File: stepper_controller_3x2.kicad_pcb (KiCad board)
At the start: 2 copper layers, 69.8 x 40.6 mm, 23 parts, among them P1 HEADER_02X05_SMD, P2 HEADER_02X05_SMD, P3 HEADER_02X05_SMD, T1 TERM_BLK_HDR_4POS_VERT_0.138IN, T2 TERM_BLK_HDR_4POS_VERT_0.138IN, T3 TERM_BLK_HDR_4POS_VERT_0.138IN, U1 TMC429, U2 26LS31, U3 MAX6817, U4 26LS31, U5 MAX6817, U6 26LS31, U7 MAX6817

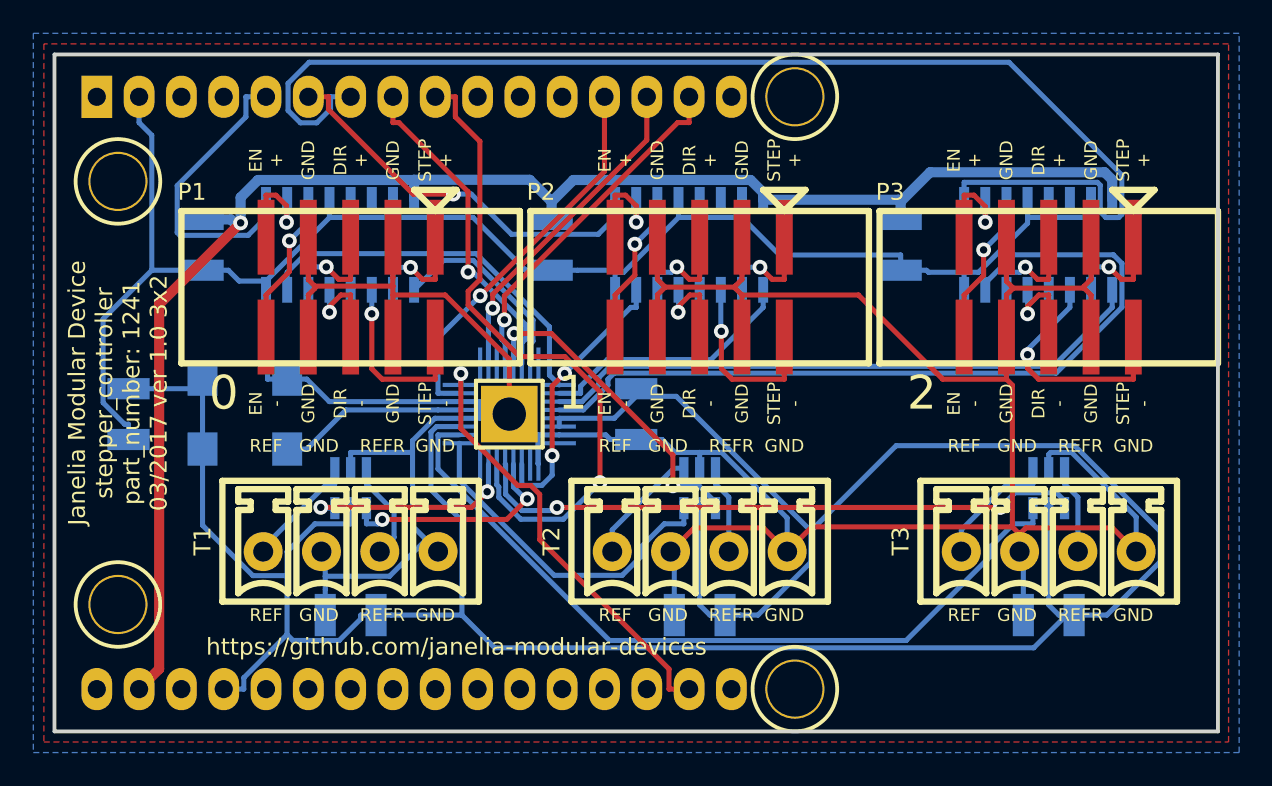
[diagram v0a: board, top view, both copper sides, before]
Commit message: Removed footprint.
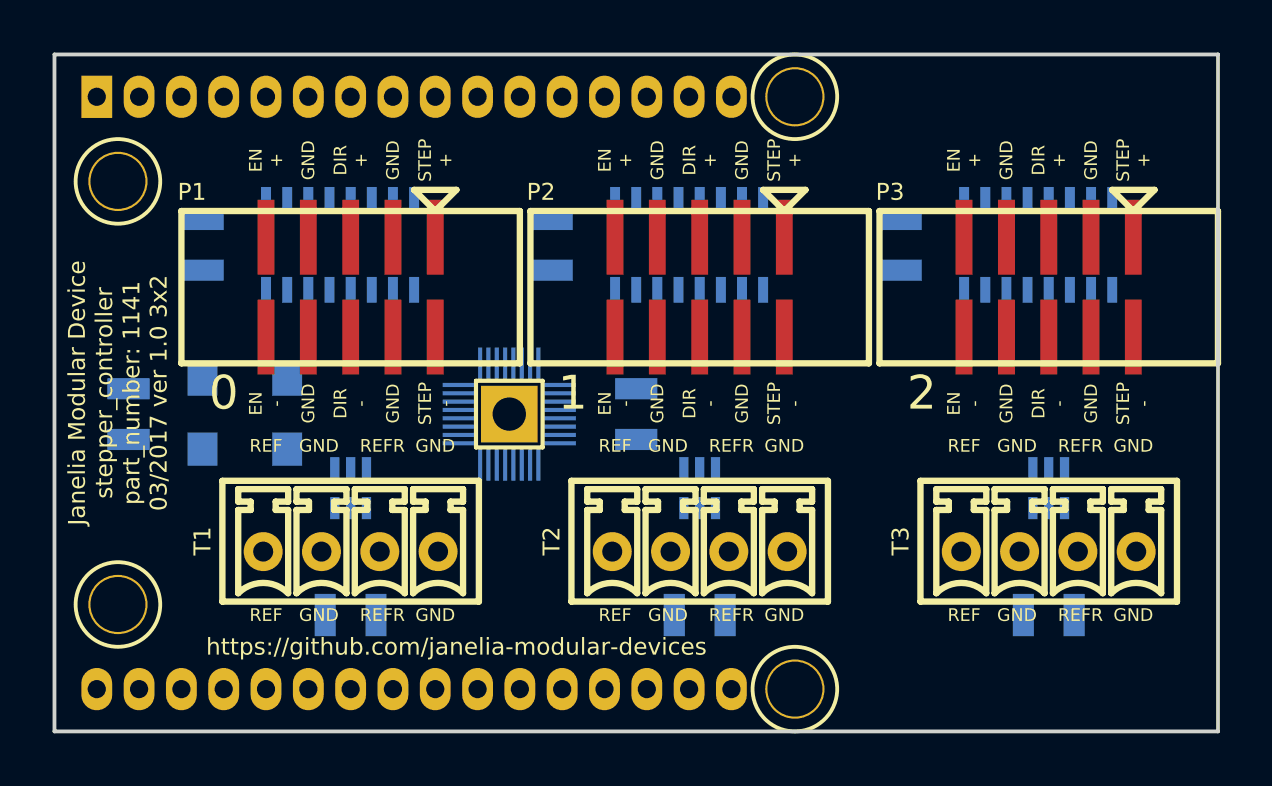
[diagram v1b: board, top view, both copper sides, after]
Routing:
- net GND: track 310.8 -> 0.00 mm
- net +3V3: track 175.5 -> 0.00 mm
- net VEE: track 94.5 -> 0.00 mm, vias 1 -> 0
- net /ENABLE_2: track 74.9 -> 0.00 mm
- net /tmc429_0/DIR_2: track 48.7 -> 0.00 mm
- net /tmc429_0/REF_2: track 47.5 -> 0.00 mm
- net /POSCOMP: track 39.7 -> 0.00 mm, vias 1 -> 0
- net /tmc429_0/REFR_2: track 36.9 -> 0.00 mm, vias 2 -> 0
- net /tmc429_0/STEP_2: track 36.8 -> 0.00 mm
- net /SCK: track 26.5 -> 0.00 mm, vias 1 -> 0
- net /ENABLE_1: track 23.7 -> 0.00 mm, vias 1 -> 0
- net /CS: track 23.2 -> 0.00 mm, vias 1 -> 0
- net /tmc429_0/DIR_0: track 22.8 -> 0.00 mm
- net /MISO: track 21.2 -> 0.00 mm, vias 1 -> 0
- net /tmc429_0/REF_1: track 20.6 -> 0.00 mm
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- removed copper zone on B.Cu, net GND
- removed copper zone on F.Cu, net GND
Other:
- board text added: "Janelia Modular Device stepper_controller part_number: 1141 03/2017 ver 1.0 3x2"
- board text removed: "Janelia Modular Device stepper_controller part_number: 1241 03/2017 ver 1.0 3x2"

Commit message: First attempt at layout.
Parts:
- removed P1, P2, P3: HEADER_02X05_SMD, stepper_controller_3x2:HEADER_02x05_SMD
- added C10: 0.1uF_0805, stepper_controller_3x2:SM0805, F.Cu at (189.3, 126.9)
- added C11: 0.47uF_0805, stepper_controller_3x2:SM0805, F.Cu at (189.6, 123.1)
- added C12: 0.1uF, stepper_controller_3x2:SM1210, F.Cu at (202.4, 111.5)
- added C13: 0.1uF_0805, stepper_controller_3x2:SM0805, F.Cu at (184.9, 98.5)
- added C14: 0.1uF_0805, stepper_controller_3x2:SM0805, F.Cu at (210.0, 86.7)
- added C15: 0.1uF_0805, stepper_controller_3x2:SM0805, F.Cu at (177.5, 98.5)
- added C16: 0.47uF_0805, stepper_controller_3x2:SM0805, F.Cu at (169.8, 98.5)
- added C17: 0.1uF, stepper_controller_3x2:SM1210, F.Cu at (209.0, 91.5)
- added C9: 0.1uF_0805, stepper_controller_3x2:SM0805, F.Cu at (203.4, 107.0)
- added T4: TERM_BLK_HDR_4POS_VERT_0.138IN, stepper_controller_3x2:TERM_BLK_HDR_4POS_VERT_0.138IN, F.Cu at (124.5, 98.4)
- added T5: TERM_BLK_HDR_4POS_VERT_0.150IN, stepper_controller_3x2:TERM_BLK_HDR_4POS_VERT_0.150IN, F.Cu at (145.4, 80.0)
- added T6: TERM_BLK_HDR_4POS_VERT_0.138IN, stepper_controller_3x2:TERM_BLK_HDR_4POS_VERT_0.138IN, F.Cu at (145.4, 98.4)
- C3, C5: value 0.1uF -> 0.1uF_0805; footprint stepper_controller_3x2:SM1210 -> stepper_controller_3x2:SM0805; moved to F.Cu
- C4, C8: value 0.1uF -> 0.1uF_0805; footprint stepper_controller_3x2:SM1210 -> stepper_controller_3x2:SM0805
- C6: value 0.1uF -> 0.47uF_0805; footprint stepper_controller_3x2:SM1210 -> stepper_controller_3x2:SM0805
- C7: moved to F.Cu
- T1, T3: value TERM_BLK_HDR_4POS_VERT_0.138IN -> TERM_BLK_HDR_4POS_VERT_0.150IN; footprint stepper_controller_3x2:TERM_BLK_HDR_4POS_VERT_0.138IN -> stepper_controller_3x2:TERM_BLK_HDR_4POS_VERT_0.150IN
- U2, U4: value 26LS31 -> TMC260; footprint stepper_controller_3x2:SOIC_16_0.154IN -> stepper_controller_3x2:TMC260+261; moved to F.Cu
- U6: value 26LS31 -> TMC260; footprint stepper_controller_3x2:SOIC_16_0.154IN -> stepper_controller_3x2:TMC260+261
- moved C3 151.4 mm to (245.9, 74.2), turned to 0 degrees
- moved U2 131.9 mm to (235.3, 77.3), turned to 0 degrees
- moved C5 130.7 mm to (245.9, 70.6), turned to 0 degrees
- moved C7 116.1 mm to (252.3, 71.5), turned to 0 degrees
- moved U4 76.2 mm to (192.8, 113.7), turned to 0 degrees
- moved T3 27.9 mm to (124.5, 80.0)
- moved U6 27.8 mm to (129.5, 57.1), turned to 0 degrees
- moved T1 21.0 mm to (103.5, 77.5)
- moved T2 21.0 mm to (103.5, 98.4)
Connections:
- net /CS renamed /CS_429
- net /tmc429_0/REFR_0 renamed /tmc429_tmc26x_0/REFR_0
- net /tmc429_0/REFR_1 renamed /tmc429_tmc26x_0/REFR_1
- net /tmc429_0/REFR_2 renamed /tmc429_tmc26x_0/REFR_2
- net /tmc429_0/REF_0 renamed /tmc429_tmc26x_0/REF_0
- net /tmc429_0/REF_1 renamed /tmc429_tmc26x_0/REF_1
- net /tmc429_0/REF_2 renamed /tmc429_tmc26x_0/REF_2
- C3 pad 1: VEE -> +3V3
- C4 pad 1: +3V3 -> VDD
- C5 pad 1: VEE -> VDD
- C5 pad 2: GND -> Net-(C5-Pad2)
- C6 pad 1: +3V3 -> Net-(C6-Pad1)
- C7 pad 1: VEE -> +3V3
- MDB1 pad 14: (no net) -> /CS_26X_0
- MDB1 pad 15: (no net) -> /CS_26X_1
- MDB1 pad 16: (no net) -> /CS_26X_2
- MDB1 pad 17: (no net) -> /SG_0
- MDB1 pad 18: (no net) -> /SG_1
- MDB1 pad 19: (no net) -> /SG_2
- MDB1 pad VDD: (no net) -> VDD
- MDB1 pad VEE: VEE -> (no net)
- T1 pad 1: /tmc429_0/stepper_0/REF_B -> /tmc429_tmc26x_0/stepper_0/A_+
- T1 pad 2: GND -> /tmc429_tmc26x_0/stepper_0/A_-
- T1 pad 3: /tmc429_0/stepper_0/REFR_B -> /tmc429_tmc26x_0/stepper_0/B_+
- T1 pad 4: GND -> /tmc429_tmc26x_0/stepper_0/B_-
- T2 pad 1: /tmc429_0/stepper_1/REF_B -> /tmc429_tmc26x_0/stepper_0/REF_B
- T2 pad 3: /tmc429_0/stepper_1/REFR_B -> /tmc429_tmc26x_0/stepper_0/REFR_B
- T3 pad 1: /tmc429_0/stepper_2/REF_B -> /tmc429_tmc26x_0/stepper_1/A_+
- T3 pad 2: GND -> /tmc429_tmc26x_0/stepper_1/A_-
- T3 pad 3: /tmc429_0/stepper_2/REFR_B -> /tmc429_tmc26x_0/stepper_1/B_+
- T3 pad 4: GND -> /tmc429_tmc26x_0/stepper_1/B_-
- U1 pad 15: /tmc429_0/STEP_0 -> /tmc429_tmc26x_0/STEP_0
- U1 pad 17: /tmc429_0/DIR_0 -> /tmc429_tmc26x_0/DIR_0
- U1 pad 18: /tmc429_0/STEP_1 -> /tmc429_tmc26x_0/STEP_1
- U1 pad 19: /tmc429_0/STEP_2 -> /tmc429_tmc26x_0/STEP_2
- U1 pad 20: /tmc429_0/DIR_2 -> /tmc429_tmc26x_0/DIR_2
- U1 pad 27: /tmc429_0/DIR_1 -> /tmc429_tmc26x_0/DIR_1
- U2 pad 1: /tmc429_0/STEP_0 -> (no net)
- U2 pad 10: /tmc429_0/stepper_0/ENABLE_+ -> /tmc429_tmc26x_0/stepper_0/A_-
- U2 pad 12: GND -> (no net)
- U2 pad 13: (no net) -> Net-(C6-Pad1)
- U2 pad 14: (no net) -> /MISO
- U2 pad 15: GND -> /MOSI
- U2 pad 16: VEE -> /SCK
- U2 pad 2: /tmc429_0/stepper_0/STEP_+ -> /tmc429_tmc26x_0/stepper_0/A_+
- U2 pad 4: (no net) -> VDD
- U2 pad 5: /tmc429_0/stepper_0/DIR_- -> /tmc429_tmc26x_0/stepper_0/A_-
- U2 pad 7: /tmc429_0/DIR_0 -> /tmc429_tmc26x_0/stepper_0/A_+
- U2 pad 9: /ENABLE_0 -> (no net)
- U3 pad 1: /tmc429_0/stepper_0/REF_B -> /tmc429_tmc26x_0/stepper_0/REF_B
- U3 pad 3: /tmc429_0/stepper_0/REFR_B -> /tmc429_tmc26x_0/stepper_0/REFR_B
- U4 pad 1: /tmc429_0/STEP_1 -> (no net)
- U4 pad 10: /tmc429_0/stepper_1/ENABLE_+ -> /tmc429_tmc26x_0/stepper_1/A_-
- U4 pad 12: GND -> (no net)
- U4 pad 13: (no net) -> Net-(C11-Pad1)
- U4 pad 14: (no net) -> /MISO
- U4 pad 15: GND -> /MOSI
- U4 pad 16: VEE -> /SCK
- U4 pad 2: /tmc429_0/stepper_1/STEP_+ -> /tmc429_tmc26x_0/stepper_1/A_+
- U4 pad 4: (no net) -> VDD
- U4 pad 5: /tmc429_0/stepper_1/DIR_- -> /tmc429_tmc26x_0/stepper_1/A_-
- U4 pad 7: /tmc429_0/DIR_1 -> /tmc429_tmc26x_0/stepper_1/A_+
- U4 pad 9: /ENABLE_1 -> (no net)
- U5 pad 1: /tmc429_0/stepper_1/REF_B -> /tmc429_tmc26x_0/stepper_1/REF_B
- U5 pad 3: /tmc429_0/stepper_1/REFR_B -> /tmc429_tmc26x_0/stepper_1/REFR_B
- U6 pad 1: /tmc429_0/STEP_2 -> (no net)
- U6 pad 10: /tmc429_0/stepper_2/ENABLE_+ -> /tmc429_tmc26x_0/stepper_2/A_-
- U6 pad 12: GND -> (no net)
- U6 pad 13: (no net) -> Net-(C16-Pad1)
- U6 pad 14: (no net) -> /MISO
- U6 pad 15: GND -> /MOSI
- U6 pad 16: VEE -> /SCK
- U6 pad 2: /tmc429_0/stepper_2/STEP_+ -> /tmc429_tmc26x_0/stepper_2/A_+
- U6 pad 4: (no net) -> VDD
- U6 pad 5: /tmc429_0/stepper_2/DIR_- -> /tmc429_tmc26x_0/stepper_2/A_-
- U6 pad 7: /tmc429_0/DIR_2 -> /tmc429_tmc26x_0/stepper_2/A_+
- U6 pad 9: /ENABLE_2 -> (no net)
- U7 pad 1: /tmc429_0/stepper_2/REF_B -> /tmc429_tmc26x_0/stepper_2/REF_B
- U7 pad 3: /tmc429_0/stepper_2/REFR_B -> /tmc429_tmc26x_0/stepper_2/REFR_B
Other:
- board text removed: "DIR +"
- board text removed: "DIR -"
- board text removed: "EN +"
- board text removed: "EN -"
- board text removed: "STEP +"
- board text removed: "STEP -"

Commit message: tmc26x -> driver.
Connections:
- net /tmc429_tmc26x_0/DIR_0 renamed /tmc429_driver_0/DIR_0
- net /tmc429_tmc26x_0/DIR_1 renamed /tmc429_driver_0/DIR_1
- net /tmc429_tmc26x_0/DIR_2 renamed /tmc429_driver_0/DIR_2
- net /tmc429_tmc26x_0/REFR_0 renamed /tmc429_driver_0/REFR_0
- net /tmc429_tmc26x_0/REFR_1 renamed /tmc429_driver_0/REFR_1
- net /tmc429_tmc26x_0/REFR_2 renamed /tmc429_driver_0/REFR_2
- net /tmc429_tmc26x_0/REF_0 renamed /tmc429_driver_0/REF_0
- net /tmc429_tmc26x_0/REF_1 renamed /tmc429_driver_0/REF_1
- net /tmc429_tmc26x_0/REF_2 renamed /tmc429_driver_0/REF_2
- net /tmc429_tmc26x_0/STEP_0 renamed /tmc429_driver_0/STEP_0
- net /tmc429_tmc26x_0/STEP_1 renamed /tmc429_driver_0/STEP_1
- net /tmc429_tmc26x_0/STEP_2 renamed /tmc429_driver_0/STEP_2
- net /tmc429_tmc26x_0/stepper_0/A_+ renamed /tmc429_driver_0/stepper_0/A_+
- net /tmc429_tmc26x_0/stepper_0/A_- renamed /tmc429_driver_0/stepper_0/A_-
- net /tmc429_tmc26x_0/stepper_0/B_+ renamed /tmc429_driver_0/stepper_0/B_+
- net /tmc429_tmc26x_0/stepper_0/B_- renamed /tmc429_driver_0/stepper_0/B_-
- net /tmc429_tmc26x_0/stepper_0/REFR_B renamed /tmc429_driver_0/stepper_0/REFR_B
- net /tmc429_tmc26x_0/stepper_0/REF_B renamed /tmc429_driver_0/stepper_0/REF_B
- net /tmc429_tmc26x_0/stepper_1/A_+ renamed /tmc429_driver_0/stepper_1/A_+
- net /tmc429_tmc26x_0/stepper_1/A_- renamed /tmc429_driver_0/stepper_1/A_-
- net /tmc429_tmc26x_0/stepper_1/B_+ renamed /tmc429_driver_0/stepper_1/B_+
- net /tmc429_tmc26x_0/stepper_1/B_- renamed /tmc429_driver_0/stepper_1/B_-
- net /tmc429_tmc26x_0/stepper_1/REFR_B renamed /tmc429_driver_0/stepper_1/REFR_B
- net /tmc429_tmc26x_0/stepper_1/REF_B renamed /tmc429_driver_0/stepper_1/REF_B
- net /tmc429_tmc26x_0/stepper_2/A_+ renamed /tmc429_driver_0/stepper_2/A_+
- net /tmc429_tmc26x_0/stepper_2/A_- renamed /tmc429_driver_0/stepper_2/A_-
- net /tmc429_tmc26x_0/stepper_2/B_+ renamed /tmc429_driver_0/stepper_2/B_+
- net /tmc429_tmc26x_0/stepper_2/B_- renamed /tmc429_driver_0/stepper_2/B_-
- net /tmc429_tmc26x_0/stepper_2/REFR_B renamed /tmc429_driver_0/stepper_2/REFR_B
- net /tmc429_tmc26x_0/stepper_2/REF_B renamed /tmc429_driver_0/stepper_2/REF_B

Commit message: Mostly finished with v1.0.
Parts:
- removed C12, C17: 0.1uF, stepper_controller_3x2:SM1210
- removed C13, C14, C15: 0.1uF_0805, stepper_controller_3x2:SM0805
- removed C16: 0.47uF_0805, stepper_controller_3x2:SM0805
- removed U5, U7: MAX6817, stepper_controller_3x2:MAX6817
- removed U6: TMC260, stepper_controller_3x2:TMC260+261
- added D1: diode_schottky_45V_10A, stepper_controller_3x2:CFP15, F.Cu at (320.0, 82.6)
- added P1: PWR_JACK_2.5x5.5, stepper_controller_3x2:DCJACK_2PIN_HIGHCURRENT, F.Cu at (155.6, 90.2)
- added SS1: STEPSTICK, stepper_controller_3x2:STEPSTICK, F.Cu at (130.8, 87.6)
- added SS2: STEPSTICK, stepper_controller_3x2:STEPSTICK, F.Cu at (273.1, 89.5)
- added SS3: STEPSTICK, stepper_controller_3x2:STEPSTICK, F.Cu at (318.6, 62.6)
- C10, C4: value 0.1uF_0805 -> 10uF; footprint stepper_controller_3x2:SM0805 -> stepper_controller_3x2:SM1210
- C11: value 0.47uF_0805 -> 0.1uF; footprint stepper_controller_3x2:SM0805 -> stepper_controller_3x2:SM1210
- C3, C9: value 0.1uF_0805 -> 100uF_POL; footprint stepper_controller_3x2:SM0805 -> stepper_controller_3x2:C_ELEC_12.5
- C5, C8: value 0.1uF_0805 -> 0.1uF; footprint stepper_controller_3x2:SM0805 -> stepper_controller_3x2:SM1210
- C6: value 0.47uF_0805 -> 100uF_POL; footprint stepper_controller_3x2:SM0805 -> stepper_controller_3x2:C_ELEC_12.5
- C7: value 0.1uF -> 10uF
- T1, T3, T5: value TERM_BLK_HDR_4POS_VERT_0.150IN -> TERM_BLK_HDR_4POS_VERT_0.2IN; footprint stepper_controller_3x2:TERM_BLK_HDR_4POS_VERT_0.150IN -> stepper_controller_3x2:TERM_BLK_HDR_4POS_VERT_0.2IN
- T2, T4, T6: value TERM_BLK_HDR_4POS_VERT_0.138IN -> TERM_BLK_HDR_4POS_VERT_0.150IN; footprint stepper_controller_3x2:TERM_BLK_HDR_4POS_VERT_0.138IN -> stepper_controller_3x2:TERM_BLK_HDR_4POS_VERT_0.150IN
- U2, U4: value TMC260 -> MAX6817; footprint stepper_controller_3x2:TMC260+261 -> stepper_controller_3x2:MAX6817
- moved C3 99.9 mm to (146.1, 77.5)
- moved T4 94.3 mm to (212.1, 63.5)
- moved T6 86.6 mm to (231.8, 92.1)
- moved T3 55.4 mm to (172.7, 52.7)
- moved T5 40.2 mm to (185.4, 76.2)
- moved C8 26.9 mm to (154.3, 127.6)
- moved C6 20.3 mm to (129.5, 121.9)
- moved T1 5.99 mm to (106.7, 82.5)
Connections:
- C10 pad 2: Net-(C10-Pad2) -> GND
- C11 pad 1: Net-(C11-Pad1) -> +3V3
- C3 pad 1: +3V3 -> VDD
- C5 pad 1: VDD -> +3V3
- C5 pad 2: Net-(C5-Pad2) -> GND
- C6 pad 1: Net-(C6-Pad1) -> VDD
- C7 pad 1: +3V3 -> VDD
- MDB1 pad 14: /CS_26X_0 -> /CS_DRIVER_0
- MDB1 pad 15: /CS_26X_1 -> /CS_DRIVER_1
- MDB1 pad 16: /CS_26X_2 -> /CS_DRIVER_2
- MDB1 pad 17: /SG_0 -> (no net)
- MDB1 pad 18: /SG_1 -> (no net)
- MDB1 pad 19: /SG_2 -> (no net)
- U2 pad 1: (no net) -> /tmc429_driver_0/stepper_0/REF_B
- U2 pad 2: /tmc429_driver_0/stepper_0/A_+ -> GND
- U2 pad 4: VDD -> /tmc429_driver_0/REFR_0
- U2 pad 5: /tmc429_driver_0/stepper_0/A_- -> +3V3
- U3 pad 1: /tmc429_driver_0/stepper_0/REF_B -> /tmc429_driver_0/stepper_1/REF_B
- U3 pad 3: /tmc429_driver_0/stepper_0/REFR_B -> /tmc429_driver_0/stepper_1/REFR_B
- U3 pad 4: /tmc429_driver_0/REFR_0 -> /tmc429_driver_0/REFR_1
- U3 pad 6: /tmc429_driver_0/REF_0 -> /tmc429_driver_0/REF_1
- U4 pad 1: (no net) -> /tmc429_driver_0/stepper_2/REF_B
- U4 pad 2: /tmc429_driver_0/stepper_1/A_+ -> GND
- U4 pad 4: VDD -> /tmc429_driver_0/REFR_2
- U4 pad 5: /tmc429_driver_0/stepper_1/A_- -> +3V3
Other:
- board text added: "Janelia Modular Device stepper_controller part_number: 1141 06/2017 ver 1.0 3x2"
- board text removed: "Janelia Modular Device stepper_controller part_number: 1141 03/2017 ver 1.0 3x2"

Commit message: Mostly finished with v1.0.
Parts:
- removed C10, C7: 10uF, stepper_controller_3x2:SM1210
- removed C11, C8: 0.1uF, stepper_controller_3x2:SM1210
- removed C6, C9: 100uF_POL, stepper_controller_3x2:C_ELEC_12.5
- removed SS2, SS3: STEPSTICK, stepper_controller_3x2:STEPSTICK
- removed T3, T5: TERM_BLK_HDR_4POS_VERT_0.2IN, stepper_controller_3x2:TERM_BLK_HDR_4POS_VERT_0.2IN
- removed T4, T6: TERM_BLK_HDR_4POS_VERT_0.150IN, stepper_controller_3x2:TERM_BLK_HDR_4POS_VERT_0.150IN
- removed U3, U4: MAX6817, stepper_controller_3x2:MAX6817
- C5, D1, U2: moved to B.Cu
- moved D1 175.9 mm to (144.1, 81.9)
- moved C5 143.8 mm to (102.9, 85.1), turned to 90 degrees
- moved U2 127.6 mm to (108.0, 85.1), turned to 270 degrees
- moved C3 37.8 mm to (112.4, 94.6), turned to 90 degrees
- moved C2 29.6 mm to (91.4, 95.2), turned to 90 degrees
- moved T1 23.6 mm to (130.2, 80.6)
- moved C4 20.8 mm to (122.6, 94.0), turned to 0 degrees
- moved T2 18.3 mm to (108.0, 80.6)
- moved U1 15.7 mm to (98.4, 95.9), turned to 180 degrees
- moved SS1 7.01 mm to (130.2, 94.6), turned to 270 degrees
- moved C1 5.24 mm to (88.9, 85.1)
- moved CLK1 5.24 mm to (95.9, 85.1)
- moved P1 1.42 mm to (156.2, 88.9)
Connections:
- MDB1 pad 15: /CS_DRIVER_1 -> (no net)
- MDB1 pad 16: /CS_DRIVER_2 -> (no net)
- MDB1 pad 3: /ENABLE_1 -> (no net)
- MDB1 pad 4: /ENABLE_2 -> (no net)
- T1 pad 1: /tmc429_driver_0/stepper_0/A_+ -> /tmc429_driver_0/stepper_0/B_-
- T1 pad 2: /tmc429_driver_0/stepper_0/A_- -> /tmc429_driver_0/stepper_0/B_+
- T1 pad 3: /tmc429_driver_0/stepper_0/B_+ -> /tmc429_driver_0/stepper_0/A_-
- T1 pad 4: /tmc429_driver_0/stepper_0/B_- -> /tmc429_driver_0/stepper_0/A_+
- U1 pad 1: /tmc429_driver_0/REF_1 -> +3V3
- U1 pad 13: /tmc429_driver_0/REFR_1 -> +3V3
- U1 pad 18: /tmc429_driver_0/STEP_1 -> (no net)
- U1 pad 19: /tmc429_driver_0/STEP_2 -> (no net)
- U1 pad 2: /tmc429_driver_0/REF_2 -> +3V3
- U1 pad 20: /tmc429_driver_0/DIR_2 -> (no net)
- U1 pad 27: /tmc429_driver_0/DIR_1 -> (no net)
- U1 pad 29: /tmc429_driver_0/REFR_2 -> +3V3
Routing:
- net GND: track 0.00 -> 142.8 mm
- net +3V3: track 0.00 -> 129.6 mm, vias 0 -> 2
- net VDD: track 0.00 -> 84.2 mm
- net /MISO: track 0.00 -> 82.9 mm
- net /MOSI: track 0.00 -> 63.2 mm, vias 0 -> 1
- net /INT: track 0.00 -> 58.6 mm
- net /tmc429_driver_0/DIR_0: track 0.00 -> 49.8 mm, vias 0 -> 1
- net /tmc429_driver_0/STEP_0: track 0.00 -> 46.0 mm, vias 0 -> 1
- net /ENABLE_0: track 0.00 -> 44.3 mm
- net /CS_429: track 0.00 -> 33.9 mm, vias 0 -> 1
- net /SCK: track 0.00 -> 32.4 mm
- net /POSCOMP: track 0.00 -> 26.4 mm, vias 0 -> 1
- net /tmc429_driver_0/REFR_0: track 0.00 -> 17.4 mm
- net /CLK: track 0.00 -> 12.3 mm, vias 0 -> 2
- net /CS_DRIVER_0: track 0.00 -> 11.5 mm
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- added copper zone on B.Cu, net GND
- added copper zone on F.Cu, net VDD
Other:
- board size 69.8 x 40.6 mm -> 70.5 x 41.9 mm
- net class SUPERPOWER: trace_width 0.6096 -> 1.27
- board text added: "2.5x5.5 Center + +9-42VDC"
- board text added: "A+"
- board text added: "A-"
- board text added: "B+"
- board text added: "B-"
- board text removed: "1"
- board text removed: "2"

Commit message: Finished v1.0.
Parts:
- C3: value 100uF_POL -> 220uF_POL; footprint stepper_controller_3x2:C_ELEC_12.5 -> stepper_controller_3x2:C_ELEC_10
- moved C1 25.9 mm to (113.7, 92.7)
- moved CLK1 13.2 mm to (106.7, 92.7), turned to 180 degrees
- moved U1 3.70 mm to (96.5, 92.7)
- moved C2 3.59 mm to (88.9, 92.7)
- moved C3 1.27 mm to (113.7, 94.6)
- moved C4 1.27 mm to (122.6, 92.7)
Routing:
- net /INT: track 58.6 -> 40.7 mm, vias 0 -> 1
- net GND: track 142.8 -> 158.4 mm
- net /MOSI: track 63.2 -> 77.9 mm, vias 1 -> 0
- net /MISO: track 82.9 -> 97.2 mm
- net +3V3: track 129.6 -> 116.1 mm
- net /CLK: track 12.3 -> 5.70 mm, vias 2 -> 0
- net /SCK: track 32.4 -> 37.5 mm
- net /ENABLE_0: track 44.3 -> 47.5 mm
- net /tmc429_driver_0/DIR_0: track 49.8 -> 53.0 mm, vias 1 -> 0
- net /CS_429: track 33.9 -> 37.1 mm
- net /CS_DRIVER_0: track 11.5 -> 13.7 mm
- net /tmc429_driver_0/STEP_0: track 46.0 -> 48.0 mm, vias 1 -> 0
- net /POSCOMP: track 26.4 -> 28.0 mm
- net VDD: track 84.2 -> 85.6 mm
- net /tmc429_driver_0/REFR_0: track 17.4 -> 16.7 mm
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- added copper zone on F.Cu, net GND
- added copper zone on B.Cu, net VDD
- removed copper zone on B.Cu, net GND
- removed copper zone on F.Cu, net VDD

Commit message: Moved footprints.
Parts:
- moved C3 0.64 mm to (113.7, 95.2)
- moved C4 0.64 mm to (122.6, 93.3)
- moved SS1 0.64 mm to (130.2, 95.2)
- moved T1 0.63 mm to (130.2, 80.0)
- moved T2 0.63 mm to (108.0, 80.0)
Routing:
- net GND: track 158.4 -> 0.00 mm
- net +3V3: track 116.1 -> 0.00 mm, vias 2 -> 0
- net /MISO: track 97.2 -> 0.00 mm
- net VDD: track 85.6 -> 0.00 mm
- net /MOSI: track 77.9 -> 0.00 mm
- net /tmc429_driver_0/DIR_0: track 53.0 -> 0.00 mm
- net /tmc429_driver_0/STEP_0: track 48.0 -> 0.00 mm
- net /ENABLE_0: track 47.5 -> 0.00 mm
- net /INT: track 40.7 -> 0.00 mm, vias 1 -> 0
- net /SCK: track 37.5 -> 0.00 mm
- net /CS_429: track 37.1 -> 0.00 mm, vias 1 -> 0
- net /POSCOMP: track 28.0 -> 0.00 mm, vias 1 -> 0
- net /tmc429_driver_0/REFR_0: track 16.7 -> 0.00 mm
- net /CS_DRIVER_0: track 13.7 -> 0.00 mm
- net /tmc429_driver_0/REF_0: track 12.0 -> 0.00 mm
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- removed copper zone on F.Cu, net GND
- removed copper zone on B.Cu, net VDD
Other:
- board text added: "2.5x5.5 Center + +12-42VDC"
- board text added: "Janelia Modular Device stepper_controller part_number: 1141 10/2017 ver 1.1 3x2"
- board text removed: "2.5x5.5 Center + +9-42VDC"
- board text removed: "Janelia Modular Device stepper_controller part_number: 1141 06/2017 ver 1.0 3x2"
